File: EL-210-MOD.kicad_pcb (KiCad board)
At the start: 2 copper layers, 66 x 65 mm, 36 parts, among them J1 Conn_01x05, J2 Conn_01x02, P1 EL-210-KEY, U1 9-ST-20, U2 STM32G0B1KET6, U3 MAX6934AQH+D, U4 TPS613221ADBV, U5 MAX4719EUB+, U6 TLV61046ADB

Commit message: Update schematics.
- Change the key matrix signal name.
-- Including the re-order of the Key row.
- Change the value of the R1 from 330 to 18.

- Schematic is generatd in PDF.
- Layout is generated in gerber.
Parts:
- R1: value 330 -> 18
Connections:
- net /KD0 renamed /KR8
- net /KD1 renamed /KR7
- net /KD2 renamed /KR6
- net /KD3 renamed /KR5
- net /KD4 renamed /KR4
- net /KD5 renamed /KR3
- net /KD6 renamed /KR2
- net /KD7 renamed /KR1
- net /KD8 renamed /KR0
- net /KEY1 renamed /KC0
- net /KEY2 renamed /KC1
- net /KEY3 renamed /KC2
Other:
- board text added: "Ver 1.0.1 (C) Seiichi Horie 2022,2023 https://github.com/suikan4github/EL-210-MOD"
- board text removed: "Ver 1.0.0 (C) Seiichi Horie 2022 https://github.com/suikan4github/EL-210-MOD"
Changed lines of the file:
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@@
   (net 60 "/EN24V")
   (net 61 "unconnected-(U2-Pad28)")
-  (net 62 "/KEY1")
-  (net 63 "/KEY2")
-  (net 64 "/KEY3")
-  (net 65 "/KD8")
-  (net 66 "/KD7")
-  (net 67 "/KD6")
-  (net 68 "/KD5")
-  (net 69 "/KD4")
-  (net 70 "/KD3")
-  (net 71 "/KD2")
-  (net 72 "/KD1")
-  (net 73 "/KD0")
+  (net 62 "/KC0")
+  (net 63 "/KC1")
+  (net 64 "/KC2")
+  (net 65 "/KR0")
+  (net 66 "/KR1")
+  (net 67 "/KR2")
+  (net 68 "/KR3")
+  (net 69 "/KR4")
+  (net 70 "/KR5")
+  (net 71 "/KR6")
+  (net 72 "/KR7")
+  (net 73 "/KR8")
   (net 74 "unconnected-(U4-Pad5)")
   (net 75 "Net-(L2-Pad1)")
@@
       (net 1 "GND") (pinfunction "GND") (pintype "power_in"))
     (pad "2" smd rect locked (at 5.5 -3.5) (size 0.5 6) (layers "B.Cu" "B.Paste" "B.Mask")
-      (net 62 "/KEY1") (pinfunction "KEY1") (pintype "output"))
+      (net 62 "/KC0") (pinfunction "KC0") (pintype "output"))
     (pad "3" smd rect locked (at 7.756 -3.5) (size 0.5 6) (layers "B.Cu" "B.Paste" "B.Mask")
-      (net 63 "/KEY2") (pinfunction "KEY2") (pintype "output"))
+      (net 63 "/KC1") (pinfunction "KC1") (pintype "output"))
     (pad "4" smd rect locked (at 10.012 -3.5) (size 0.5 6) (layers "B.Cu" "B.Paste" "B.Mask")
-      (net 64 "/KEY3") (pinfunction "KEY3") (pintype "output"))
+      (net 64 "/KC2") (pinfunction "KC2") (pintype "output"))
     (pad "5" smd rect locked (at 12.268 -3.5) (size 0.5 6) (layers "B.Cu" "B.Paste" "B.Mask")
-      (net 65 "/KD8") (pinfunction "D8") (pintype "input"))
+      (net 65 "/KR0") (pinfunction "KR0") (pintype "input"))
     (pad "6" smd rect locked (at 14.524 -3.5) (size 0.5 6) (layers "B.Cu" "B.Paste" "B.Mask")
-      (net 66 "/KD7") (pinfunction "D7") (pintype "input"))
+      (net 66 "/KR1") (pinfunction "KR1") (pintype "input"))
     (pad "7" smd rect locked (at 16.78 -3.5) (size 0.5 6) (layers "B.Cu" "B.Paste" "B.Mask")
-      (net 67 "/KD6") (pinfunction "D6") (pintype "input"))
+      (net 67 "/KR2") (pinfunction "KR2") (pintype "input"))
     (pad "8" smd rect locked (at 19.036 -3.5) (size 0.5 6) (layers "B.Cu" "B.Paste" "B.Mask")
-      (net 68 "/KD5") (pinfunction "D5") (pintype "input"))
+      (net 68 "/KR3") (pinfunction "KR3") (pintype "input"))
     (pad "9" smd rect locked (at 21.292 -3.5) (size 0.5 6) (layers "B.Cu" "B.Paste" "B.Mask")
-      (net 69 "/KD4") (pinfunction "D4") (pintype "input"))
+      (net 69 "/KR4") (pinfunction "KR4") (pintype "input"))
     (pad "10" smd rect locked (at 23.548 -3.5) (size 0.5 6) (layers "B.Cu" "B.Paste" "B.Mask")
-      (net 70 "/KD3") (pinfunction "D3") (pintype "input"))
+      (net 70 "/KR5") (pinfunction "KR5") (pintype "input"))
     (pad "11" smd rect locked (at 25.804 -3.5) (size 0.5 6) (layers "B.Cu" "B.Paste" "B.Mask")
-      (net 71 "/KD2") (pinfunction "D2") (pintype "input"))
+      (net 71 "/KR6") (pinfunction "KR6") (pintype "input"))
     (pad "12" smd rect locked (at 32.2 -3.5) (size 0.5 6) (layers "B.Cu" "B.Paste" "B.Mask")
       (net 2 "unconnected-(P1-Pad12)") (pinfunction "NC") (pintype "no_connect"))
     (pad "13" smd rect locked (at 34.3 -3.5) (size 0.5 6) (layers "B.Cu" "B.Paste" "B.Mask")
-      (net 72 "/KD1") (pinfunction "D1") (pintype "input"))
+      (net 72 "/KR7") (pinfunction "KR7") (pintype "input"))
     (pad "14" smd rect locked (at 36.58 -3.5) (size 0.5 6) (layers "B.Cu" "B.Paste" "B.Mask")
-      (net 73 "/KD0") (pinfunction "D0") (pintype "input"))
+      (net 73 "/KR8") (pinfunction "KR8") (pintype "input"))
     (pad "15" smd rect locked (at 38.86 -3.5) (size 0.5 6) (layers "B.Cu" "B.Paste" "B.Mask")
       (net 1 "GND") (pinfunction "GND") (pintype "power_in"))
@@
       (effects (font (size 1 1) (thickness 0.15)))
     )
-    (fp_text value "330" (at 0 1.43 90) (layer "F.Fab") hide
+    (fp_text value "18" (at 0 1.43 90) (layer "F.Fab") hide
       (effects (font (size 1 1) (thickness 0.15)))
     )
@@
       (net 52 "/NRST") (pinfunction "PF2-NRST") (pintype "passive"))
     (pad "7" smd roundrect (at -4.175 2) (size 1.5 0.5) (layers "F.Cu" "F.Paste" "F.Mask") (roundrect_rratio 0.25)
-      (net 62 "/KEY1") (pinfunction "PA0") (pintype "bidirectional"))
+      (net 62 "/KC0") (pinfunction "PA0") (pintype "bidirectional"))
     (pad "8" smd roundrect (at -4.175 2.8) (size 1.5 0.5) (layers "F.Cu" "F.Paste" "F.Mask") (roundrect_rratio 0.25)
-      (net 63 "/KEY2") (pinfunction "PA1") (pintype "bidirectional"))
+      (net 63 "/KC1") (pinfunction "PA1") (pintype "bidirectional"))
     (pad "9" smd roundrect (at -2.8 4.175) (size 0.5 1.5) (layers "F.Cu" "F.Paste" "F.Mask") (roundrect_rratio 0.25)
-      (net 64 "/KEY3") (pinfunction "PA2") (pintype "bidirectional"))
+      (net 64 "/KC2") (pinfunction "PA2") (pintype "bidirectional"))
     (pad "10" smd roundrect (at -2 4.175) (size 0.5 1.5) (layers "F.Cu" "F.Paste" "F.Mask") (roundrect_rratio 0.25)
-      (net 65 "/KD8") (pinfunction "PA3") (pintype "bidirectional"))
+      (net 65 "/KR0") (pinfunction "PA3") (pintype "bidirectional"))
     (pad "11" smd roundrect (at -1.2 4.175) (size 0.5 1.5) (layers "F.Cu" "F.Paste" "F.Mask") (roundrect_rratio 0.25)
-      (net 66 "/KD7") (pinfunction "PA4") (pintype "bidirectional"))
+      (net 66 "/KR1") (pinfunction "PA4") (pintype "bidirectional"))
     (pad "12" smd roundrect (at -0.4 4.175) (size 0.5 1.5) (layers "F.Cu" "F.Paste" "F.Mask") (roundrect_rratio 0.25)
-      (net 67 "/KD6") (pinfunction "PA5") (pintype "bidirectional"))
+      (net 67 "/KR2") (pinfunction "PA5") (pintype "bidirectional"))
     (pad "13" smd roundrect (at 0.4 4.175) (size 0.5 1.5) (layers "F.Cu" "F.Paste" "F.Mask") (roundrect_rratio 0.25)
-      (net 68 "/KD5") (pinfunction "PA6") (pintype "bidirectional"))
+      (net 68 "/KR3") (pinfunction "PA6") (pintype "bidirectional"))
     (pad "14" smd roundrect (at 1.2 4.175) (size 0.5 1.5) (layers "F.Cu" "F.Paste" "F.Mask") (roundrect_rratio 0.25)
       (net 53 "/TIM1_CH1N") (pinfunction "PA7") (pintype "bidirectional"))
     (pad "15" smd roundrect (at 2 4.175) (size 0.5 1.5) (layers "F.Cu" "F.Paste" "F.Mask") (roundrect_rratio 0.25)
-      (net 69 "/KD4") (pinfunction "PB0") (pintype "bidirectional"))
+      (net 69 "/KR4") (pinfunction "PB0") (pintype "bidirectional"))
     (pad "16" smd roundrect (at 2.8 4.175) (size 0.5 1.5) (layers "F.Cu" "F.Paste" "F.Mask") (roundrect_rratio 0.25)
-      (net 70 "/KD3") (pinfunction "PB1") (pintype "bidirectional"))
+      (net 70 "/KR5") (pinfunction "PB1") (pintype "bidirectional"))
     (pad "17" smd roundrect (at 4.175 2.8) (size 1.5 0.5) (layers "F.Cu" "F.Paste" "F.Mask") (roundrect_rratio 0.25)
-      (net 71 "/KD2") (pinfunction "PB2") (pintype "bidirectional"))
+      (net 71 "/KR6") (pinfunction "PB2") (pintype "bidirectional"))
     (pad "18" smd roundrect (at 4.175 2) (size 1.5 0.5) (layers "F.Cu" "F.Paste" "F.Mask") (roundrect_rratio 0.25)
       (net 54 "/TIM1_CH1") (pinfunction "PA8") (pintype "bidirectional"))
@@
       (net 80 "/TIM1_CH2") (pinfunction "PA9") (pintype "bidirectional"))
     (pad "20" smd roundrect (at 4.175 0.4) (size 1.5 0.5) (layers "F.Cu" "F.Paste" "F.Mask") (roundrect_rratio 0.25)
-      (net 72 "/KD1") (pinfunction "PC6") (pintype "bidirectional"))
+      (net 72 "/KR7") (pinfunction "PC6") (pintype "bidirectional"))
     (pad "21" smd roundrect (at 4.175 -0.4) (size 1.5 0.5) (layers "F.Cu" "F.Paste" "F.Mask") (roundrect_rratio 0.25)
-      (net 73 "/KD0") (pinfunction "PA10") (pintype "bidirectional"))
+      (net 73 "/KR8") (pinfunction "PA10") (pintype "bidirectional"))
     (pad "22" smd roundrect (at 4.175 -1.2) (size 1.5 0.5) (layers "F.Cu" "F.Paste" "F.Mask") (roundrect_rratio 0.25)
       (net 43 "/LOAD") (pinfunction "PA11_PA9") (pintype "bidirectional"))
@@
     (effects (font (size 1.5 1.5) (thickness 0.3)))
   )
-  (gr_text "Ver 1.0.0\n(C) Seiichi Horie 2022\nhttps://github.com/suikan4github/EL-210-MOD" (at 180.595 129.11 90) (layer "F.SilkS")
+  (gr_text "Ver 1.0.1\n(C) Seiichi Horie 2022,2023\nhttps://github.com/suikan4github/EL-210-MOD" (at 180.594991 129.110003 90) (layer "F.SilkS")
     (effects (font (size 1 1) (thickness 0.15)) (justify left))
   )

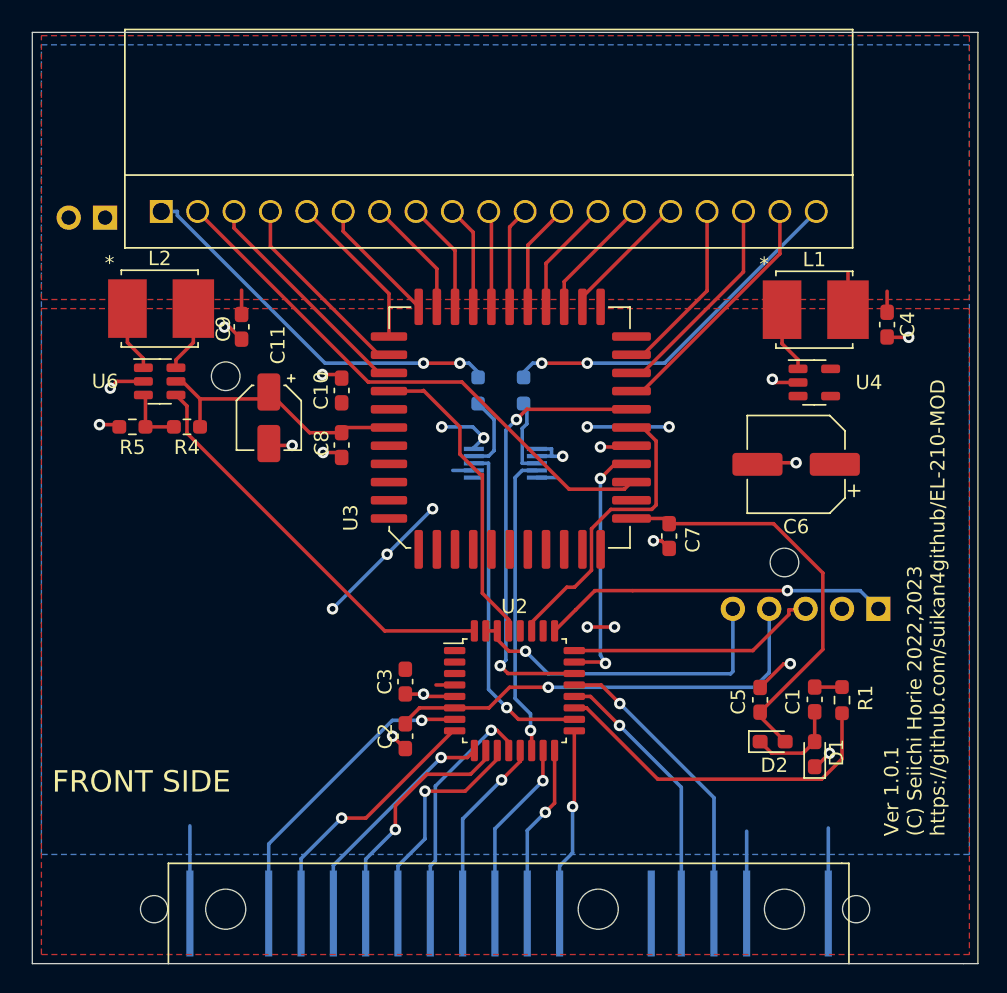
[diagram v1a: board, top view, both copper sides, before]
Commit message: Refresh the layout.
Regenerated the gerber for v1.0.1
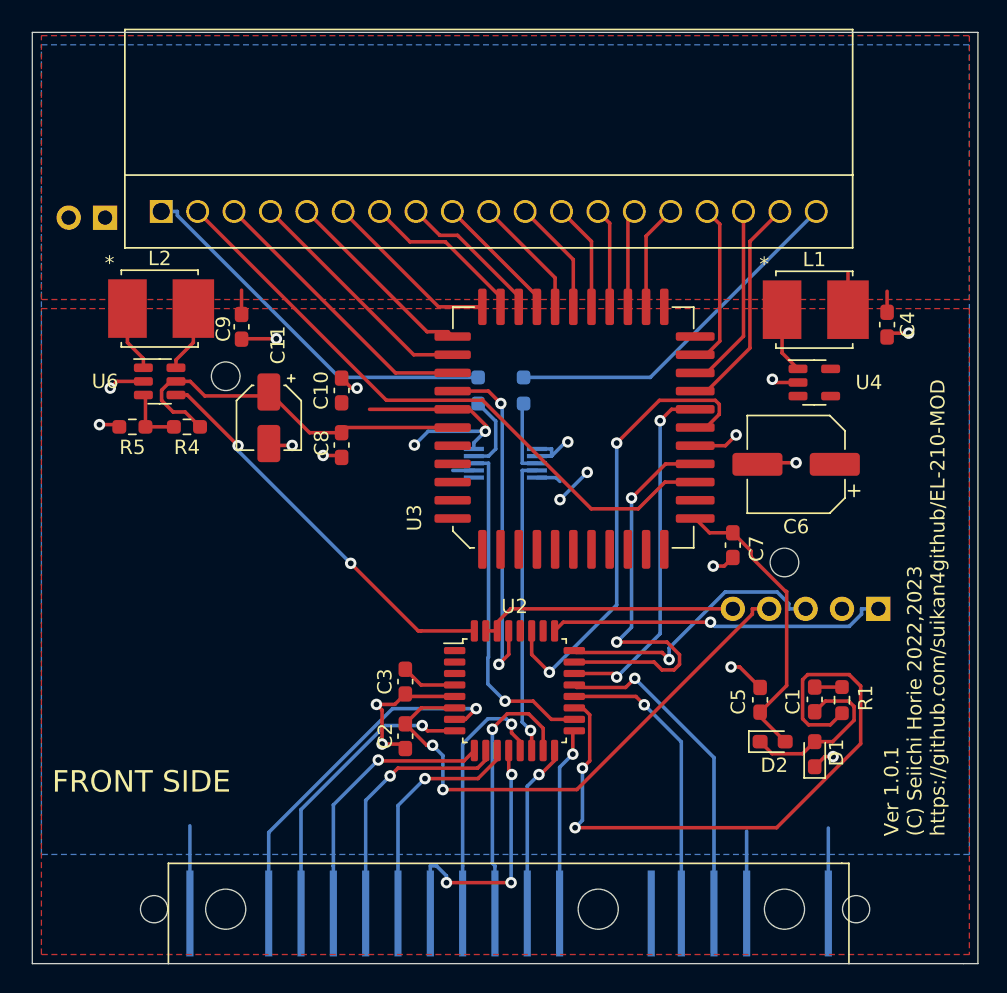
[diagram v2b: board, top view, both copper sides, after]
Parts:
- moved C7 4.49 mm to (167.9, 108.8)
- moved U3 4.44 mm to (156.5, 100.5)
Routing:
- net /TIM1_CH2: track 24.5 -> 46.5 mm, vias 0 -> 2
- net /SPI1_SCK: track 21.0 -> 32.6 mm, vias 0 -> 2
- net /BLANK: track 18.1 -> 29.1 mm
- net -2V5: track 29.2 -> 20.7 mm
- net +24V: track 18.9 -> 26.7 mm
- net /NRST: track 31.4 -> 38.0 mm, vias 1 -> 2
- net /LOAD: track 31.4 -> 25.0 mm
- net GND: track 51.3 -> 57.6 mm, vias 17 -> 15
- net /KR4: track 12.8 -> 18.9 mm
- net /SEG_A: track 38.5 -> 44.1 mm
- net Net-(C1-Pad2): track 6.56 -> 12.1 mm
- net /KR3: track 13.0 -> 18.2 mm
- net /LPUART2_TX: track 23.3 -> 18.2 mm, vias 1 -> 0
- net /KC0: track 21.4 -> 25.5 mm
- net Net-(U1-Pad3): track 16.2 -> 19.9 mm
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
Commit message: Fixed foot print of the C6 and C11.
The foot prints of those capacitor was wrong.
Corrected them.
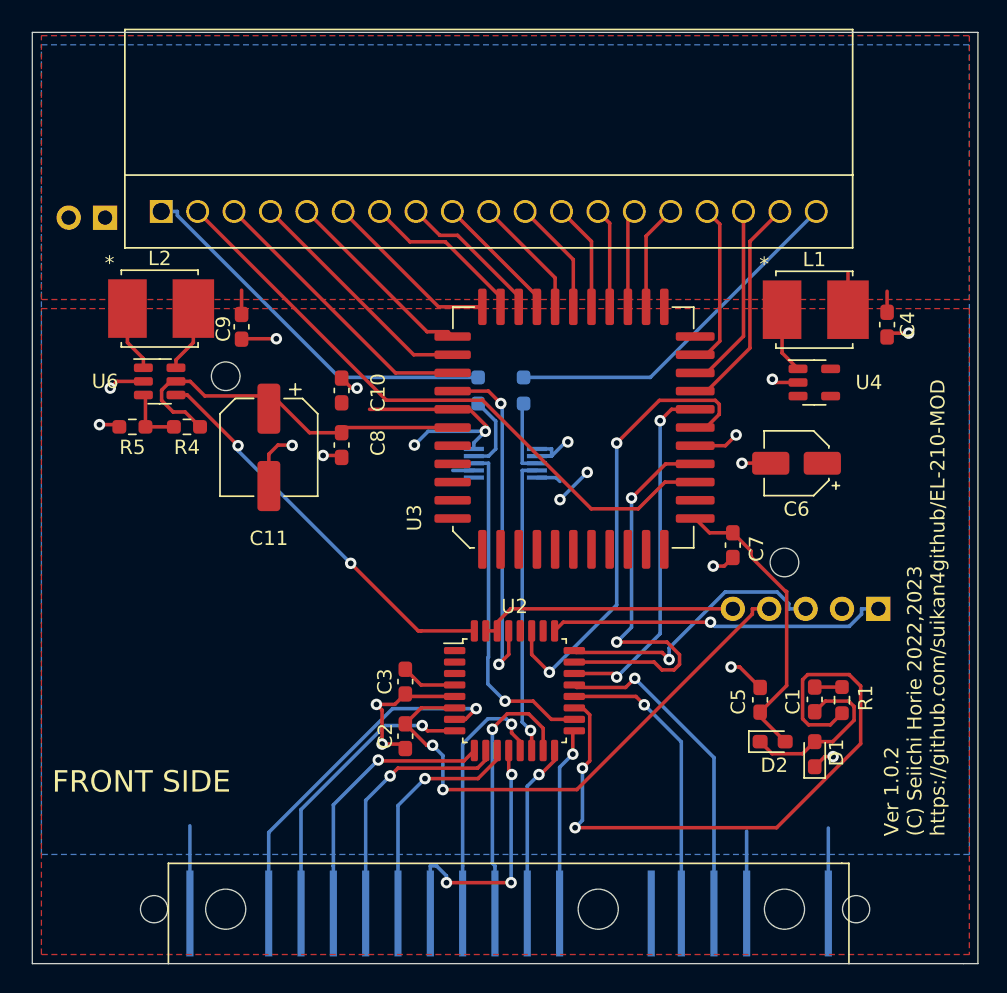
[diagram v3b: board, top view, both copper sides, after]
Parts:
- C11: footprint Capacitor_SMD:CP_Elec_4x3.9 -> Capacitor_SMD:CP_Elec_6.3x3.9
- C6: footprint Capacitor_SMD:CP_Elec_6.3x3.9 -> Capacitor_SMD:CP_Elec_4x3.9
- moved C11 2.06 mm to (135.5, 102.0)
- moved C6 0.08 mm to (172.3, 103.1)
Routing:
- net GND: track 57.6 -> 59.1 mm
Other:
- board text added: "Ver 1.0.2 (C) Seiichi Horie 2022,2023 https://github.com/suikan4github/EL-210-MOD"
- board text removed: "Ver 1.0.1 (C) Seiichi Horie 2022,2023 https://github.com/suikan4github/EL-210-MOD"
